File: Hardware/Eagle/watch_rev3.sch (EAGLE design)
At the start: 36 parts

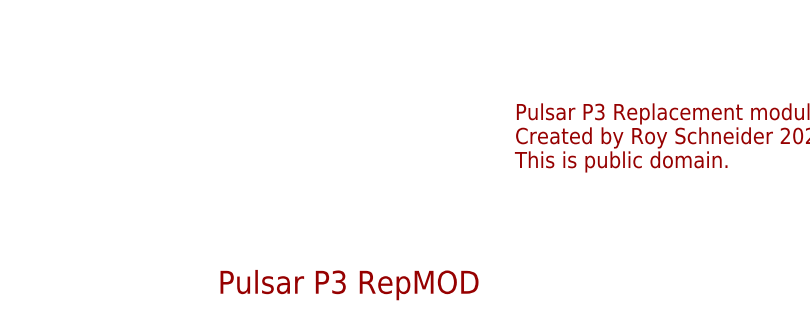
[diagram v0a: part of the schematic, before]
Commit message: Optimized layout for manual soldering.
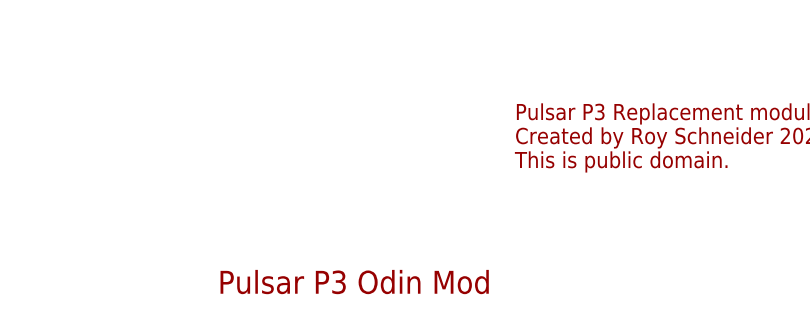
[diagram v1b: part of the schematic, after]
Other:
- note added: "Pulsar P3 Odin Mod"
- note removed: "Pulsar P3 RepMOD"
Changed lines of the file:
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@@
 Created by Roy Schneider 2020.
 This is public domain.</text>
-<text x="-22.86" y="-110.49" size="2.54" layer="94" font="vector">Pulsar P3 RepMOD</text>
+<text x="-22.86" y="-110.49" size="2.54" layer="94" font="vector">Pulsar P3 Odin Mod</text>
 <text x="-20.32" y="27.94" size="1.778" layer="94">If using a photo diode,
 instead of the vintage

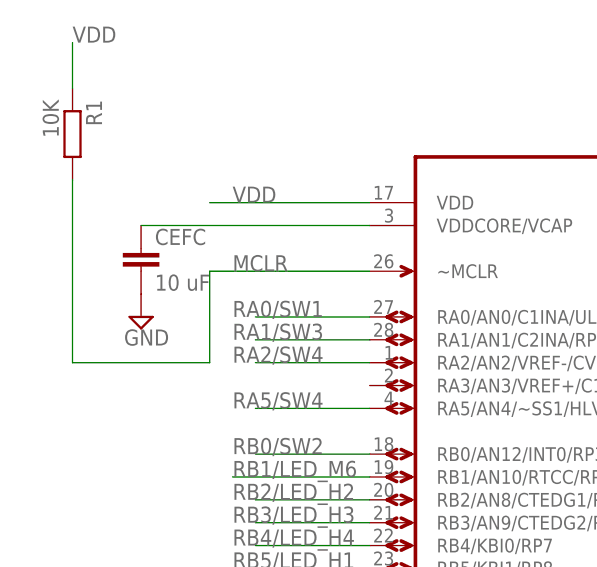
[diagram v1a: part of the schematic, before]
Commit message: Updated resitor values and fine tuned some traces.
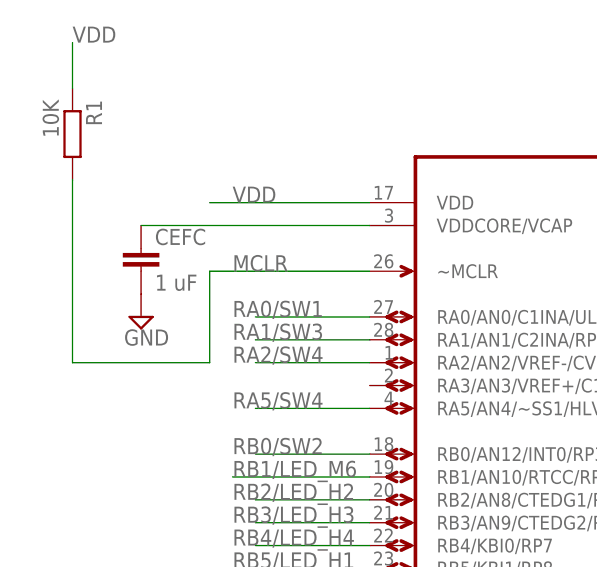
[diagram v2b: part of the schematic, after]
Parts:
- CEFC: value 10 uF -> 1 uF
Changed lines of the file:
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@@
 <part name="R1" library="rcl" deviceset="R-EU_" device="R0402" value="10K"/>
 <part name="C2" library="resistor" deviceset="C-EU" device="C0603" value="0.1 uF"/>
-<part name="CEFC" library="resistor" deviceset="C-EU" device="C0603" value="10 uF"/>
+<part name="CEFC" library="resistor" deviceset="C-EU" device="C0603" value="1 uF"/>
 <part name="SUPPLY2" library="supply2" deviceset="GND" device=""/>
 <part name="SUPPLY3" library="supply2" deviceset="GND" device=""/>

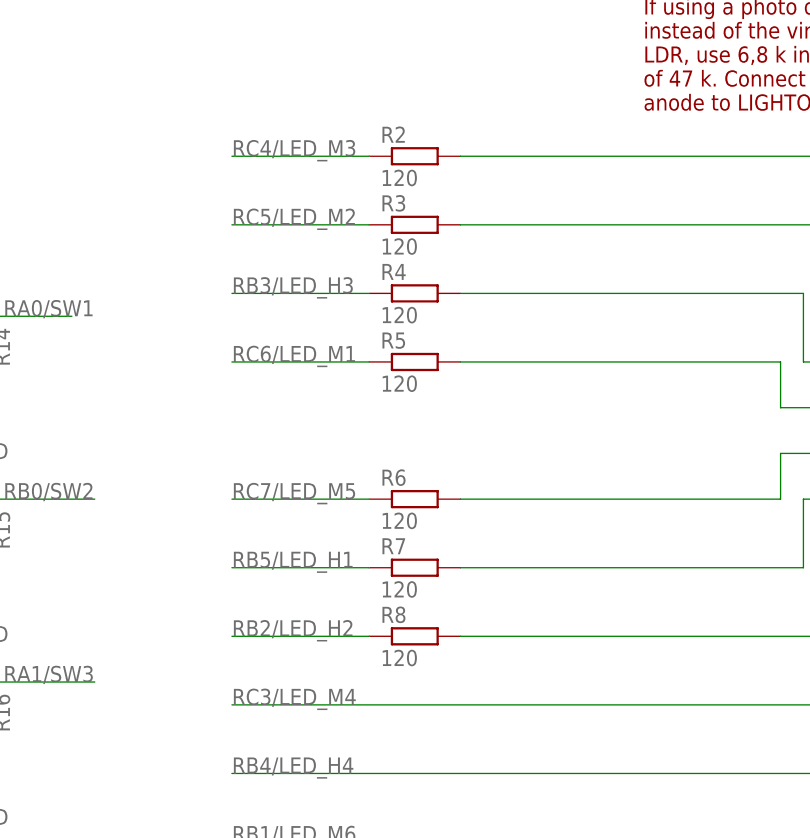
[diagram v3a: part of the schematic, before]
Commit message: Fixed resistor value.
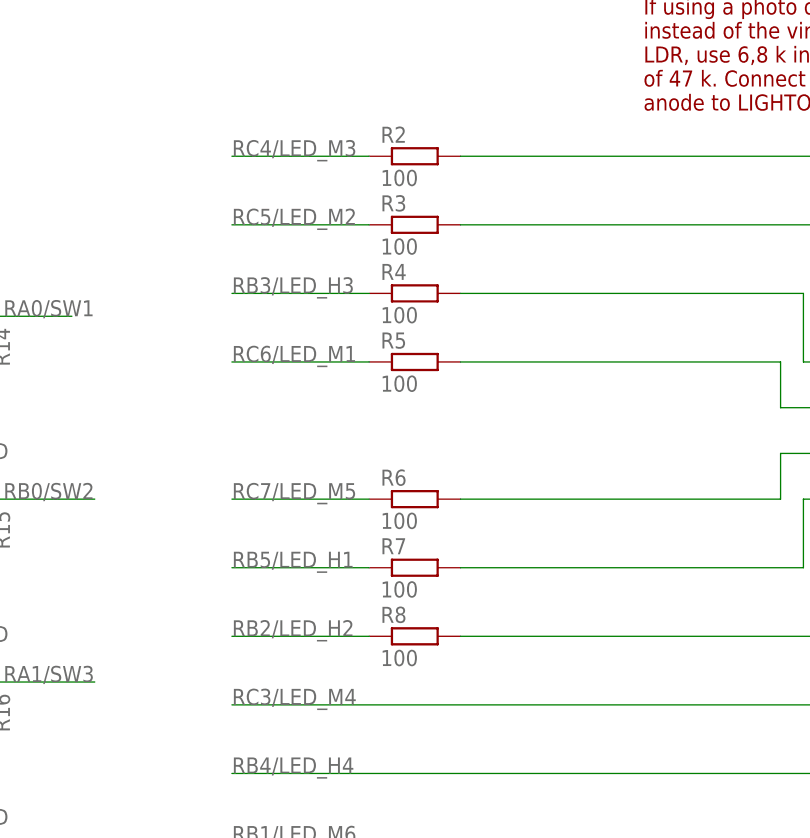
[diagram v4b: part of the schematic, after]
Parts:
- R2, R3, R4, R5, R6, R7, R8: value 120 -> 100
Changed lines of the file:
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@@
 <part name="SUPPLY2" library="supply2" deviceset="GND" device=""/>
 <part name="SUPPLY3" library="supply2" deviceset="GND" device=""/>
-<part name="R2" library="resistor" deviceset="R-EU_" device="R0402" value="120"/>
-<part name="R3" library="resistor" deviceset="R-EU_" device="R0402" value="120"/>
-<part name="R4" library="resistor" deviceset="R-EU_" device="R0402" value="120"/>
-<part name="R5" library="resistor" deviceset="R-EU_" device="R0402" value="120"/>
-<part name="R6" library="resistor" deviceset="R-EU_" device="R0402" value="120"/>
-<part name="R7" library="resistor" deviceset="R-EU_" device="R0402" value="120"/>
-<part name="R8" library="resistor" deviceset="R-EU_" device="R0402" value="120"/>
+<part name="R2" library="resistor" deviceset="R-EU_" device="R0402" value="100"/>
+<part name="R3" library="resistor" deviceset="R-EU_" device="R0402" value="100"/>
+<part name="R4" library="resistor" deviceset="R-EU_" device="R0402" value="100"/>
+<part name="R5" library="resistor" deviceset="R-EU_" device="R0402" value="100"/>
+<part name="R6" library="resistor" deviceset="R-EU_" device="R0402" value="100"/>
+<part name="R7" library="resistor" deviceset="R-EU_" device="R0402" value="100"/>
+<part name="R8" library="resistor" deviceset="R-EU_" device="R0402" value="100"/>
 <part name="R14" library="resistor" deviceset="R-EU_" device="R0402" value="4.7k"/>
 <part name="R15" library="resistor" deviceset="R-EU_" device="R0402" value="4.7k"/>

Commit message: Updated pdf files.
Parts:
- R2, R3, R4, R5, R6, R7, R8: value 100 -> 82
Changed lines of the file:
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@@
 <part name="SUPPLY2" library="supply2" deviceset="GND" device=""/>
 <part name="SUPPLY3" library="supply2" deviceset="GND" device=""/>
-<part name="R2" library="resistor" deviceset="R-EU_" device="R0402" value="100"/>
-<part name="R3" library="resistor" deviceset="R-EU_" device="R0402" value="100"/>
-<part name="R4" library="resistor" deviceset="R-EU_" device="R0402" value="100"/>
-<part name="R5" library="resistor" deviceset="R-EU_" device="R0402" value="100"/>
-<part name="R6" library="resistor" deviceset="R-EU_" device="R0402" value="100"/>
-<part name="R7" library="resistor" deviceset="R-EU_" device="R0402" value="100"/>
-<part name="R8" library="resistor" deviceset="R-EU_" device="R0402" value="100"/>
+<part name="R2" library="resistor" deviceset="R-EU_" device="R0402" value="82"/>
+<part name="R3" library="resistor" deviceset="R-EU_" device="R0402" value="82"/>
+<part name="R4" library="resistor" deviceset="R-EU_" device="R0402" value="82"/>
+<part name="R5" library="resistor" deviceset="R-EU_" device="R0402" value="82"/>
+<part name="R6" library="resistor" deviceset="R-EU_" device="R0402" value="82"/>
+<part name="R7" library="resistor" deviceset="R-EU_" device="R0402" value="82"/>
+<part name="R8" library="resistor" deviceset="R-EU_" device="R0402" value="82"/>
 <part name="R14" library="resistor" deviceset="R-EU_" device="R0402" value="4.7k"/>
 <part name="R15" library="resistor" deviceset="R-EU_" device="R0402" value="4.7k"/>

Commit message: Reviewed.
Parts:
- CEFC: value 1 uF -> 4.7-10 uF
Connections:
- removed net RA2/SW4: U$1.RA2/AN2/VREF-/CVREF/C2INB
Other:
- moved on the sheet: CEFC, R1
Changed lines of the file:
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@@
 <part name="R1" library="rcl" deviceset="R-EU_" device="R0402" value="10K"/>
 <part name="C2" library="resistor" deviceset="C-EU" device="C0603" value="0.1 uF"/>
-<part name="CEFC" library="resistor" deviceset="C-EU" device="C0603" value="1 uF"/>
+<part name="CEFC" library="resistor" deviceset="C-EU" device="C0603" value="4.7-10 uF"/>
 <part name="SUPPLY2" library="supply2" deviceset="GND" device=""/>
 <part name="SUPPLY3" library="supply2" deviceset="GND" device=""/>
@@
 <instances>
 <instance part="U$1" gate="A" x="-27.94" y="88.9"/>
-<instance part="R1" gate="G$1" x="-116.84" y="121.92" rot="R270"/>
+<instance part="R1" gate="G$1" x="-119.38" y="121.92" rot="R270"/>
 <instance part="C2" gate="G$1" x="-93.98" y="50.8" rot="R180"/>
-<instance part="CEFC" gate="G$1" x="-109.22" y="109.22"/>
-<instance part="SUPPLY2" gate="GND" x="-109.22" y="101.6"/>
+<instance part="CEFC" gate="G$1" x="-114.3" y="109.22"/>
+<instance part="SUPPLY2" gate="GND" x="-114.3" y="101.6"/>
 <instance part="SUPPLY3" gate="GND" x="-104.14" y="53.34"/>
 <instance part="R2" gate="G$1" x="-45.72" y="22.86"/>
@@
 <wire x1="-83.82" y1="106.68" x2="-101.6" y2="106.68" width="0.1524" layer="91"/>
 <wire x1="-101.6" y1="106.68" x2="-101.6" y2="96.52" width="0.1524" layer="91"/>
-<wire x1="-101.6" y1="96.52" x2="-116.84" y2="96.52" width="0.1524" layer="91"/>
+<wire x1="-101.6" y1="96.52" x2="-119.38" y2="96.52" width="0.1524" layer="91"/>
 <label x="-99.06" y="106.68" size="1.778" layer="95"/>
 <pinref part="R1" gate="G$1" pin="2"/>
-<wire x1="-116.84" y1="96.52" x2="-116.84" y2="116.84" width="0.1524" layer="91"/>
+<wire x1="-119.38" y1="96.52" x2="-119.38" y2="116.84" width="0.1524" layer="91"/>
 </segment>
 <segment>
@@
 <segment>
 <pinref part="R1" gate="G$1" pin="1"/>
-<wire x1="-116.84" y1="127" x2="-116.84" y2="132.08" width="0.1524" layer="91"/>
-<label x="-116.84" y="132.08" size="1.778" layer="95"/>
+<wire x1="-119.38" y1="127" x2="-119.38" y2="132.08" width="0.1524" layer="91"/>
+<label x="-119.38" y="132.08" size="1.778" layer="95"/>
 </segment>
 <segment>
@@
 </segment>
 </net>
-<net name="RA2/SW4" class="0">
-<segment>
-<pinref part="U$1" gate="A" pin="RA2/AN2/VREF-/CVREF/C2INB"/>
-<wire x1="-83.82" y1="96.52" x2="-96.52" y2="96.52" width="0.1524" layer="91"/>
-<label x="-99.06" y="96.52" size="1.778" layer="95"/>
-</segment>
-</net>
 <net name="VDDCORE/VCAP" class="0">
 <segment>
 <pinref part="U$1" gate="A" pin="VDDCORE/VCAP"/>
 <pinref part="CEFC" gate="G$1" pin="1"/>
-<wire x1="-83.82" y1="111.76" x2="-109.22" y2="111.76" width="0.1524" layer="91"/>
-</segment>
-</net>
+<wire x1="-83.82" y1="111.76" x2="-114.3" y2="111.76" width="0.1524" layer="91"/>
+</segment>
+</net>
